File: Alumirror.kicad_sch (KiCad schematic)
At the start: 42 parts, among them J1 USB_C_Receptacle_USB2.0_16P_2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, J2 USB_C_Receptacle_USB2.0_16P_2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, J3 USB_C_Receptacle_USB2.0_16P_2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, J4 USB_C_Receptacle_USB2.0_16P_2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, SW10 BOOT, U1 CH552T, U2 CH552T, U3 USBLC6-2P6, U4 USBLC6-2P6, U5 USBLC6-2P6, U6 USBLC6-2P6

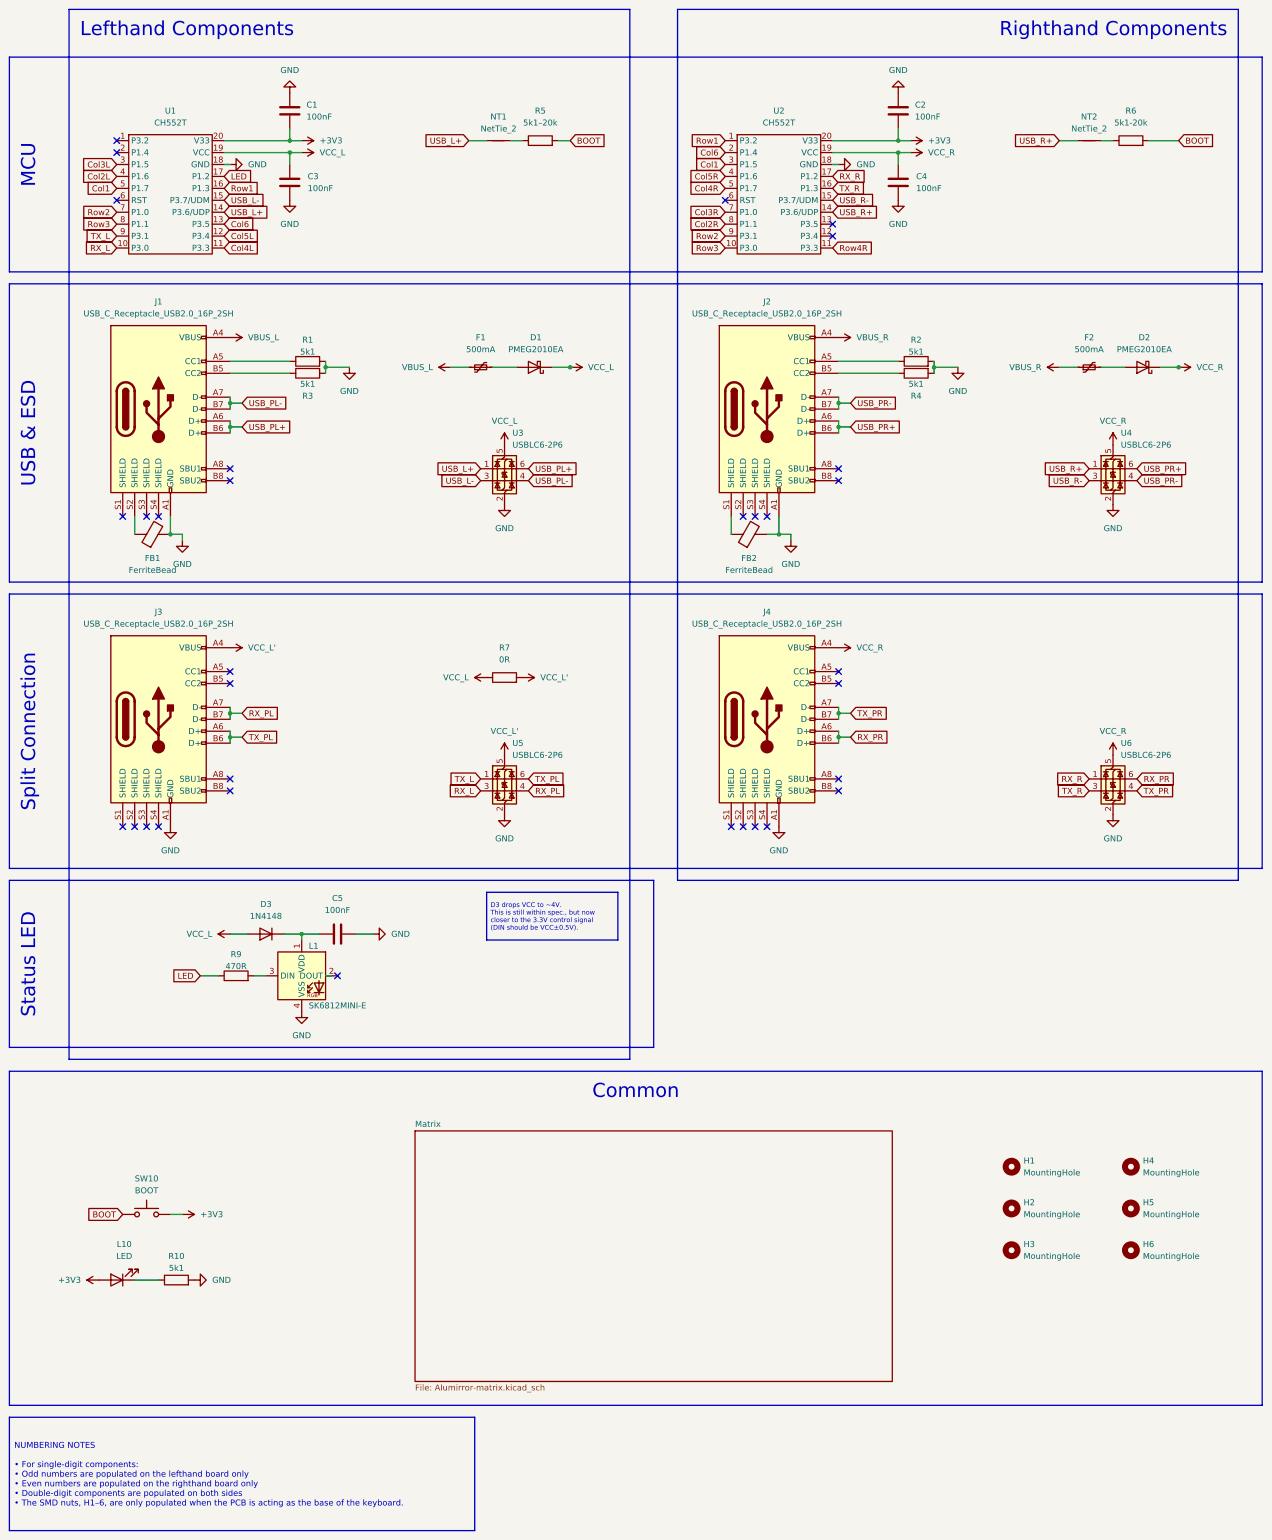
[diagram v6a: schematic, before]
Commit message: Test left-hand only components, outline and routing
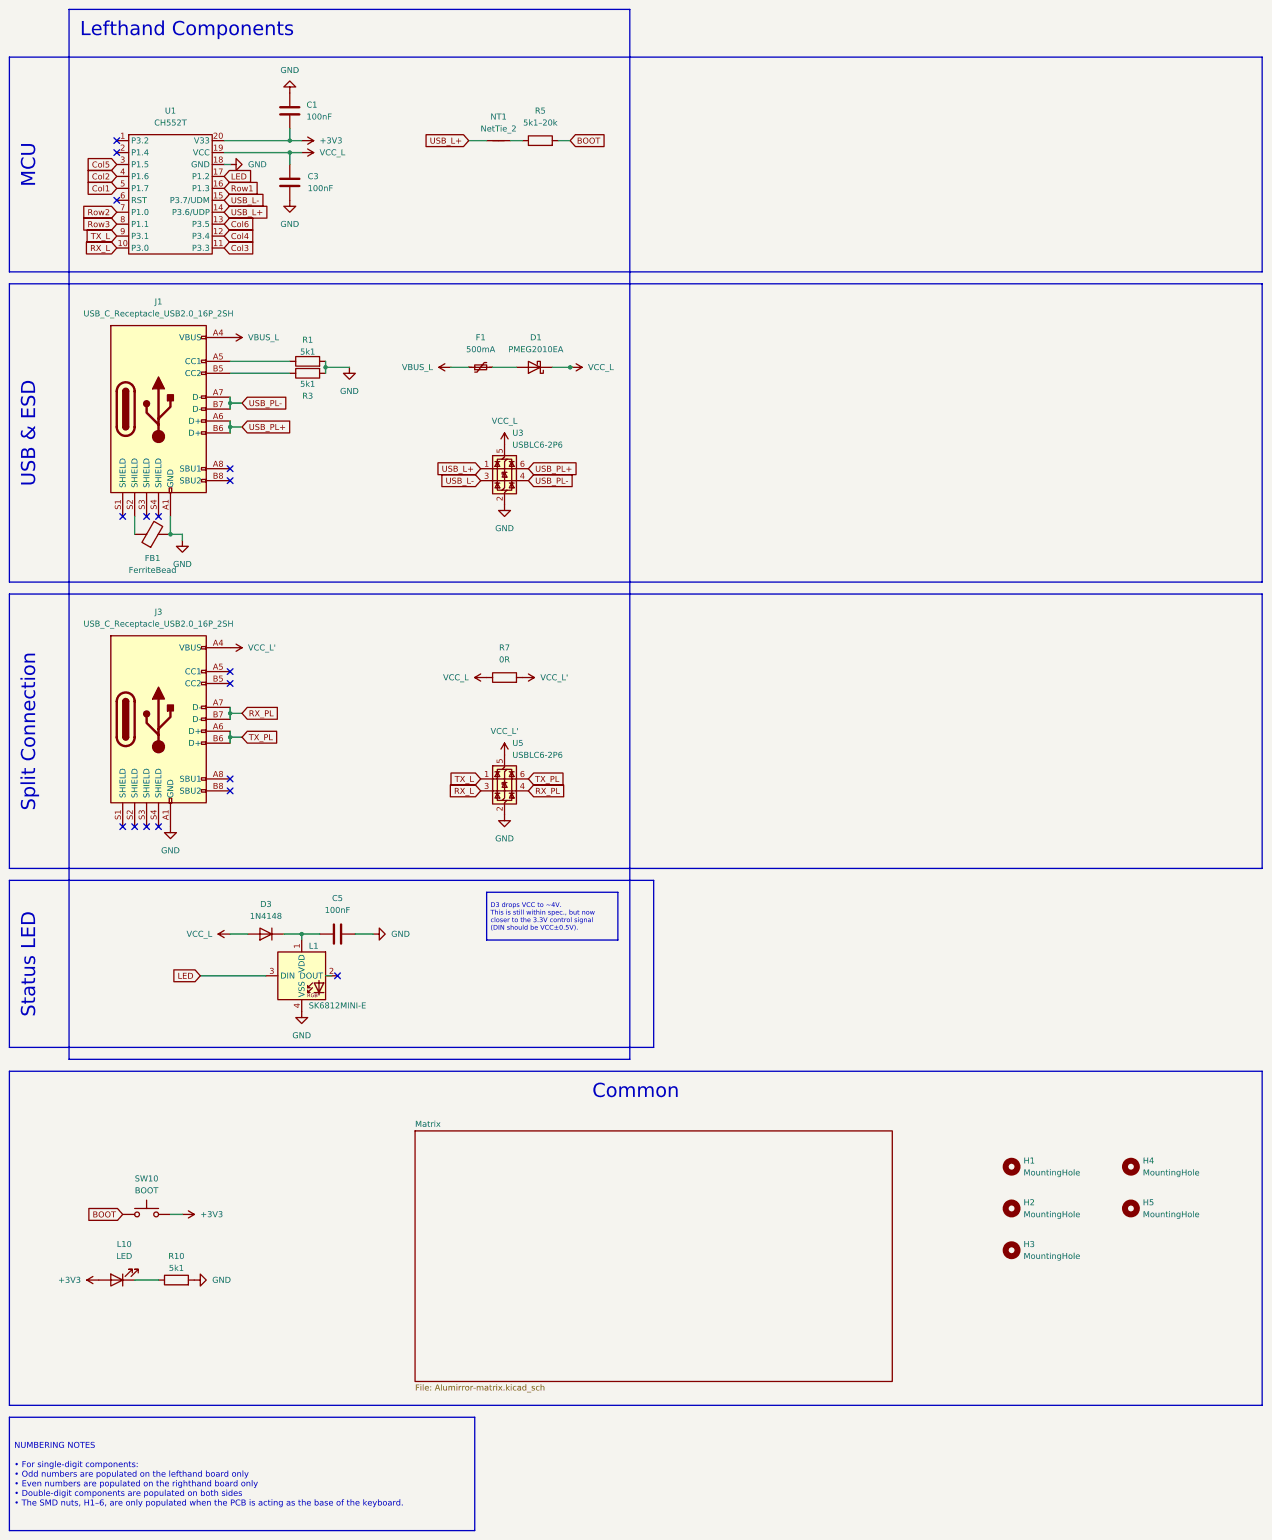
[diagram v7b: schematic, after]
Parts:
- removed C2, C4: 100nF, Capacitor_SMD:C_0603_1608Metric, symbol Device:C
- removed D2: PMEG2010EA, Diode_SMD:D_SOD-323, symbol Device:D_Schottky
- removed F2: 500mA, Fuse:Fuse_0603_1608Metric, symbol Device:Polyfuse_Small
- removed FB2: FerriteBead, Inductor_SMD:L_0805_2012Metric, symbol Device:FerriteBead
- removed H6: MountingHole, Project Library:MountingHole_2.2mm_M2_SMD_Solder_Nut, symbol Mechanical:MountingHole
- removed J2, J4: USB_C_Receptacle_USB2.0_16P_2SH, Project Library:USB_C_Receptacle_HRO_TYPE-C-31-M-12, symbol Project Library:USB_C_Receptacle_USB2.0_16P_2SH
- removed NT2: NetTie_2, Project Library:NetTie-2_SMD_Pad0.2mm, symbol Device:NetTie_2
- removed R2, R4: 5k1, Resistor_SMD:R_0603_1608Metric, symbol Device:R
- removed R6: 5k1-20k, Resistor_SMD:R_0603_1608Metric, symbol Device:R
- removed R9: 470R, Resistor_SMD:R_0805_2012Metric, symbol Device:R
- removed U2: CH552T, Package_SO:TSSOP-20_4.4x6.5mm_P0.65mm, symbol Project Library:MCU_CH552T_TSSOP-20
- removed U4, U6: USBLC6-2P6, Project Library:SOT-666_Mod, symbol Power_Protection:USBLC6-2P6
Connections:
- net LED: now also L1.3 (DIN)
- net Col2L renamed Col2
- net Col3L renamed Col5
- net Col4L renamed Col3
- net Col5L renamed Col4
- no-connect marks 33 -> 17

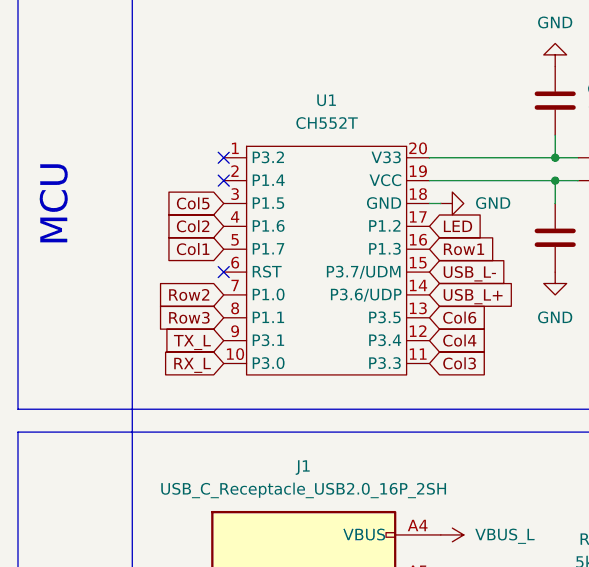
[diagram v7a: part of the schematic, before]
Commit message: Change thumb keys to columns 1 and 6
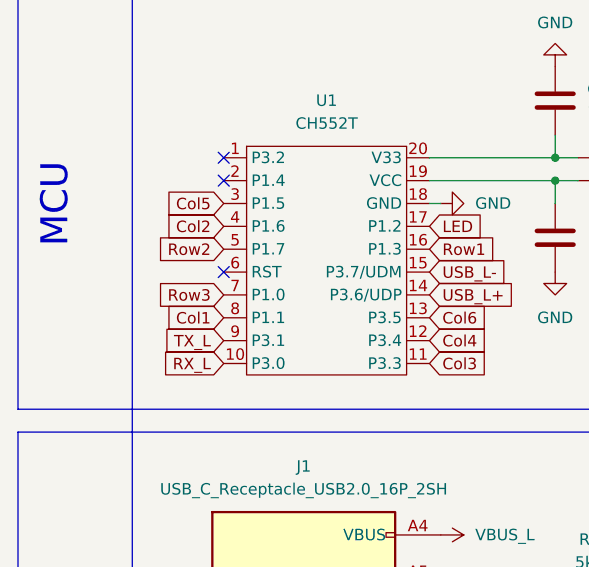
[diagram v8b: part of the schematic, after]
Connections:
- net Col1: now also U1.8 (P1.1); no longer U1.5 (P1.7)
- net Row2: now also U1.5 (P1.7); no longer U1.7 (P1.0)
- net Row3: now also U1.7 (P1.0); no longer U1.8 (P1.1)
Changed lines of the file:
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@@
 	(global_label "Col1"
 		(shape input)
-		(at 38.1 53.34 180)
+		(at 38.1 60.96 180)
 		(fields_autoplaced yes)
 		(effects
@@
 		)
 		(property "Intersheetrefs" "${INTERSHEET_REFS}"
-			(at 30.8211 53.34 0)
+			(at 30.8211 60.96 0)
 			(effects
 				(font
@@
 	(global_label "Row3"
 		(shape input)
-		(at 38.1 60.96 180)
+		(at 38.1 58.42 180)
 		(fields_autoplaced yes)
 		(effects
@@
 		)
 		(property "Intersheetrefs" "${INTERSHEET_REFS}"
-			(at 30.1558 60.96 0)
+			(at 30.1558 58.42 0)
 			(effects
 				(font
@@
 	(global_label "Row2"
 		(shape input)
-		(at 38.1 58.42 180)
+		(at 38.1 53.34 180)
 		(fields_autoplaced yes)
 		(effects
@@
 		)
 		(property "Intersheetrefs" "${INTERSHEET_REFS}"
-			(at 30.1558 58.42 0)
+			(at 30.1558 53.34 0)
 			(effects
 				(font
